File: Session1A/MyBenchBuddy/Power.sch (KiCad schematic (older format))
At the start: 11 parts

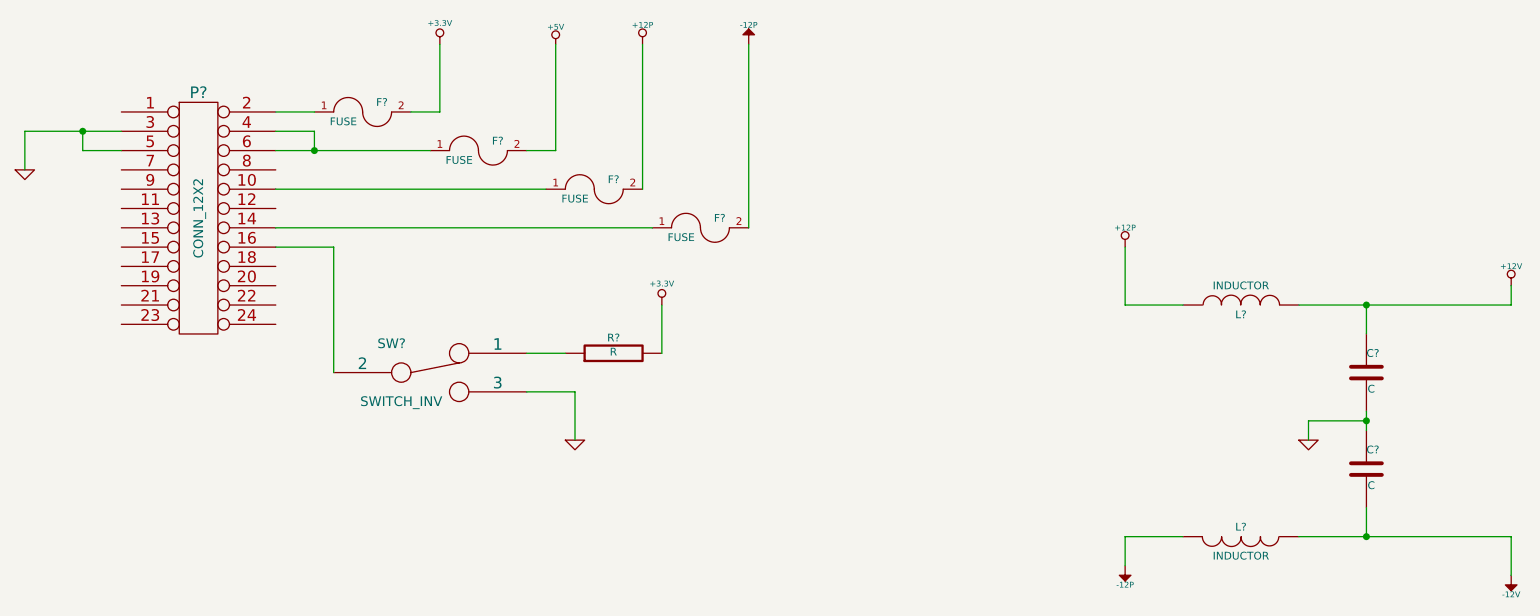
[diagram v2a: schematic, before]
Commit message: Revisiting The Current/Fan Module
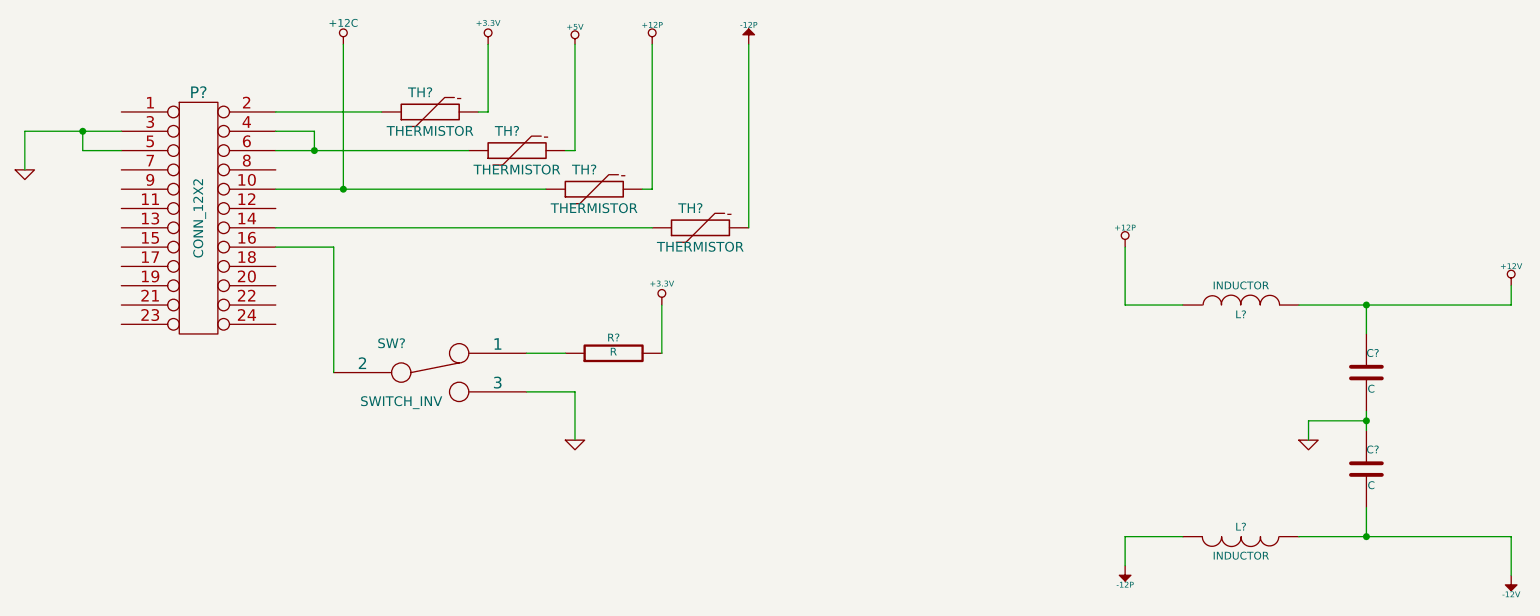
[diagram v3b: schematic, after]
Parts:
- removed F? (x4): FUSE, ~, symbol FUSE
- added TH? (x4): THERMISTOR, ~, symbol THERMISTOR
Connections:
- net +12P: now also TH?.2
- net +3.3V: now also TH?.2
- net +5V: now also TH?.2
- net -12P: now also TH?.2
- net +12C: now reaches P?.10 (P10)
- net +12C: now also TH?.1
- net at P?.14 (P14): now also TH?.1
- net at P?.2 (P2): now also TH?.1
- net at P?.4 (P4), P?.6 (P6): now also TH?.1
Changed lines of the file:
@@
 $Descr A4 11693 8268
 encoding utf-8
-Sheet 5 9
+Sheet 3 9
 Title ""
-Date "26 feb 2014"
+Date "1 mar 2014"
 Rev ""
 Comp ""
@@
 $EndComp
 Wire Wire Line
-	1400 1550 900  1550
+	900  1550 1400 1550
 Wire Wire Line
 	900  1550 900  1750
@@
 L +3.3V #PWR?
 U 1 1 52F9B474
-P 3050 1100
-F 0 "#PWR?" H 3050 1060 30  0001 C CNN
-F 1 "+3.3V" H 3050 1210 30  0000 C CNN
-F 2 "" H 3050 1100 60  0000 C CNN
-F 3 "" H 3050 1100 60  0000 C CNN
-	1    3050 1100
+P 3300 1100
+F 0 "#PWR?" H 3300 1060 30  0001 C CNN
+F 1 "+3.3V" H 3300 1210 30  0000 C CNN
+F 2 "" H 3300 1100 60  0000 C CNN
+F 3 "" H 3300 1100 60  0000 C CNN
+	1    3300 1100
 	1    0    0    -1
 $EndComp
@@
 L +5V #PWR?
 U 1 1 52F9B617
-P 3650 1100
-F 0 "#PWR?" H 3650 1190 20  0001 C CNN
-F 1 "+5V" H 3650 1190 30  0000 C CNN
-F 2 "" H 3650 1100 60  0000 C CNN
-F 3 "" H 3650 1100 60  0000 C CNN
-	1    3650 1100
-	1    0    0    -1
-$EndComp
-$Comp
-L FUSE F?
-U 1 1 52F9BC63
-P 2650 1450
-F 0 "F?" H 2750 1500 40  0000 C CNN
-F 1 "FUSE" H 2550 1400 40  0000 C CNN
-F 2 "~" H 2650 1450 60  0000 C CNN
-F 3 "~" H 2650 1450 60  0000 C CNN
-	1    2650 1450
-	1    0    0    -1
-$EndComp
-$Comp
-L FUSE F?
-U 1 1 52F9BC70
-P 3250 1650
-F 0 "F?" H 3350 1700 40  0000 C CNN
-F 1 "FUSE" H 3150 1600 40  0000 C CNN
-F 2 "~" H 3250 1650 60  0000 C CNN
-F 3 "~" H 3250 1650 60  0000 C CNN
-	1    3250 1650
-	1    0    0    -1
-$EndComp
-$Comp
-L FUSE F?
-U 1 1 52F9BC76
-P 3850 1850
-F 0 "F?" H 3950 1900 40  0000 C CNN
-F 1 "FUSE" H 3750 1800 40  0000 C CNN
-F 2 "~" H 3850 1850 60  0000 C CNN
-F 3 "~" H 3850 1850 60  0000 C CNN
-	1    3850 1850
-	1    0    0    -1
-$EndComp
-$Comp
-L FUSE F?
-U 1 1 52F9BC7C
-P 4400 2050
-F 0 "F?" H 4500 2100 40  0000 C CNN
-F 1 "FUSE" H 4300 2000 40  0000 C CNN
-F 2 "~" H 4400 2050 60  0000 C CNN
-F 3 "~" H 4400 2050 60  0000 C CNN
-	1    4400 2050
+P 3750 1100
+F 0 "#PWR?" H 3750 1190 20  0001 C CNN
+F 1 "+5V" H 3750 1190 30  0000 C CNN
+F 2 "" H 3750 1100 60  0000 C CNN
+F 3 "" H 3750 1100 60  0000 C CNN
+	1    3750 1100
 	1    0    0    -1
 $EndComp
@@
 $EndComp
 Wire Wire Line
-	2200 1450 2400 1450
-Wire Wire Line
-	2900 1450 3050 1450
-Wire Wire Line
-	3050 1450 3050 1100
+	2200 1450 2750 1450
+Wire Wire Line
+	3250 1450 3300 1450
 Wire Wire Line
 	2200 1550 2400 1550
@@
 	2400 1550 2400 1650
 Wire Wire Line
-	2200 1650 3000 1650
+	2200 1650 3200 1650
 Connection ~ 2400 1650
 Wire Wire Line
-	3500 1650 3650 1650
-Wire Wire Line
-	3650 1650 3650 1100
+	3700 1650 3750 1650
 Wire Wire Line
 	2200 1850 3600 1850
 Wire Wire Line
 	4150 2050 2200 2050
-Wire Wire Line
-	4100 1850 4100 1100
 Wire Wire Line
 	4650 2050 4650 1100
@@
 L +12P #PWR?
 U 1 1 52F9C39A
-P 4100 1100
-F 0 "#PWR?" H 4100 1070 30  0001 C CNN
-F 1 "+12P" H 4100 1200 30  0000 C CNN
-F 2 "" H 4100 1100 60  0000 C CNN
-F 3 "" H 4100 1100 60  0000 C CNN
-	1    4100 1100
+P 4150 1100
+F 0 "#PWR?" H 4150 1070 30  0001 C CNN
+F 1 "+12P" H 4150 1200 30  0000 C CNN
+F 2 "" H 4150 1100 60  0000 C CNN
+F 3 "" H 4150 1100 60  0000 C CNN
+	1    4150 1100
 	1    0    0    -1
 $EndComp
@@
 	7500 3650 8600 3650
 Wire Wire Line
-	7850 3100 7850 3000
+	7850 3000 7850 3100
 Wire Wire Line
 	6900 2450 6600 2450
@@
 	-1   0    0    1
 $EndComp
+Wire Wire Line
+	3300 1450 3300 1100
+Wire Wire Line
+	2550 1850 2550 1100
+Connection ~ 2550 1850
+$Comp
+L +12C #PWR?
+U 1 1 53118C21
+P 2550 1100
+F 0 "#PWR?" H 2550 1070 30  0001 C CNN
+F 1 "+12C" H 2550 1210 40  0000 C CNN
+F 2 "" H 2550 1100 60  0000 C CNN
+F 3 "" H 2550 1100 60  0000 C CNN
+	1    2550 1100
+	1    0    0    -1
+$EndComp
+Wire Wire Line
+	3750 1650 3750 1100
+$Comp
+L THERMISTOR TH?
+U 1 1 53119958
+P 3000 1450
+F 0 "TH?" V 3100 1500 50  0000 C CNN
+F 1 "THERMISTOR" V 2900 1450 50  0000 C CNN
+F 2 "~" H 3000 1450 60  0000 C CNN
+F 3 "~" H 3000 1450 60  0000 C CNN
+	1    3000 1450
+	0    -1   -1   0
+$EndComp
+$Comp
+L THERMISTOR TH?
+U 1 1 531199C4
+P 3450 1650
+F 0 "TH?" V 3550 1700 50  0000 C CNN
+F 1 "THERMISTOR" V 3350 1650 50  0000 C CNN
+F 2 "~" H 3450 1650 60  0000 C CNN
+F 3 "~" H 3450 1650 60  0000 C CNN
+	1    3450 1650
+	0    -1   -1   0
+$EndComp
+$Comp
+L THERMISTOR TH?
+U 1 1 531199CA
+P 3850 1850
+F 0 "TH?" V 3950 1900 50  0000 C CNN
+F 1 "THERMISTOR" V 3750 1850 50  0000 C CNN
+F 2 "~" H 3850 1850 60  0000 C CNN
+F 3 "~" H 3850 1850 60  0000 C CNN
+	1    3850 1850
+	0    -1   -1   0
+$EndComp
+$Comp
+L THERMISTOR TH?
+U 1 1 531199D0
+P 4400 2050
+F 0 "TH?" V 4500 2100 50  0000 C CNN
+F 1 "THERMISTOR" V 4300 2050 50  0000 C CNN
+F 2 "~" H 4400 2050 60  0000 C CNN
+F 3 "~" H 4400 2050 60  0000 C CNN
+	1    4400 2050
+	0    -1   -1   0
+$EndComp
+Wire Wire Line
+	4150 1100 4150 1850
+Wire Wire Line
+	4150 1850 4100 1850
 $EndSCHEMATC

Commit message: initial
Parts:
- gave numbers to parts that had none: 11
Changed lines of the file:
@@
 Sheet 3 9
 Title ""
-Date "1 mar 2014"
+Date "15 mar 2014"
 Rev ""
 Comp ""
@@
 $EndDescr
 $Comp
-L CONN_12X2 P?
+L CONN_12X2 P1
 U 1 1 52F9B2D8
 P 1800 2000
-F 0 "P?" H 1800 2650 60  0000 C CNN
+F 0 "P1" H 1800 2650 60  0000 C CNN
 F 1 "CONN_12X2" V 1800 2000 50  0000 C CNN
 F 2 "" H 1800 2000 60  0000 C CNN
@@
 	900  1550 900  1750
 $Comp
-L GND #PWR?
+L GND #PWR3
 U 1 1 52F9B2F7
 P 900 1750
-F 0 "#PWR?" H 900 1750 30  0001 C CNN
+F 0 "#PWR3" H 900 1750 30  0001 C CNN
 F 1 "GND" H 900 1680 30  0001 C CNN
 F 2 "" H 900 1750 60  0000 C CNN
@@
 $EndComp
 $Comp
-L +3.3V #PWR?
+L +3.3V #PWR5
 U 1 1 52F9B474
 P 3300 1100
-F 0 "#PWR?" H 3300 1060 30  0001 C CNN
+F 0 "#PWR5" H 3300 1060 30  0001 C CNN
 F 1 "+3.3V" H 3300 1210 30  0000 C CNN
 F 2 "" H 3300 1100 60  0000 C CNN
@@
 $EndComp
 $Comp
-L +5V #PWR?
+L +5V #PWR6
 U 1 1 52F9B617
 P 3750 1100
-F 0 "#PWR?" H 3750 1190 20  0001 C CNN
+F 0 "#PWR6" H 3750 1190 20  0001 C CNN
 F 1 "+5V" H 3750 1190 30  0000 C CNN
 F 2 "" H 3750 1100 60  0000 C CNN
@@
 $EndComp
 $Comp
-L SWITCH_INV SW?
+L SWITCH_INV SW1
 U 1 1 52F9BE18
 P 3000 2800
-F 0 "SW?" H 2800 2950 50  0000 C CNN
+F 0 "SW1" H 2800 2950 50  0000 C CNN
 F 1 "SWITCH_INV" H 2850 2650 50  0000 C CNN
 F 2 "~" H 3000 2800 60  0000 C CNN
@@
 	4650 2050 4650 1100
 $Comp
-L +12P #PWR?
+L +12P #PWR8
 U 1 1 52F9C39A
 P 4150 1100
-F 0 "#PWR?" H 4150 1070 30  0001 C CNN
+F 0 "#PWR8" H 4150 1070 30  0001 C CNN
 F 1 "+12P" H 4150 1200 30  0000 C CNN
 F 2 "" H 4150 1100 60  0000 C CNN
@@
 $EndComp
 $Comp
-L -12P #PWR?
+L -12P #PWR10
 U 1 1 52F9C3A9
 P 4650 1100
-F 0 "#PWR?" H 4650 1230 20  0001 C CNN
+F 0 "#PWR10" H 4650 1230 20  0001 C CNN
 F 1 "-12P" H 4650 1200 30  0000 C CNN
 F 2 "" H 4650 1100 60  0000 C CNN
@@
 	3750 2900 3750 3150
 $Comp
-L GND #PWR?
+L GND #PWR7
 U 1 1 52F9CAE5
 P 3750 3150
-F 0 "#PWR?" H 3750 3150 30  0001 C CNN
+F 0 "#PWR7" H 3750 3150 30  0001 C CNN
 F 1 "GND" H 3750 3080 30  0001 C CNN
 F 2 "" H 3750 3150 60  0000 C CNN
@@
 $EndComp
 $Comp
-L R R?
+L R R7
 U 1 1 52F9CE4D
 P 3950 2700
-F 0 "R?" V 4030 2700 40  0000 C CNN
+F 0 "R7" V 4030 2700 40  0000 C CNN
 F 1 "R" V 3957 2701 40  0000 C CNN
 F 2 "~" V 3880 2700 30  0000 C CNN
@@
 	4200 2700 4200 2450
 $Comp
-L +3.3V #PWR?
+L +3.3V #PWR9
 U 1 1 52F9CE88
 P 4200 2450
-F 0 "#PWR?" H 4200 2410 30  0001 C CNN
+F 0 "#PWR9" H 4200 2410 30  0001 C CNN
 F 1 "+3.3V" H 4200 2560 30  0000 C CNN
 F 2 "" H 4200 2450 60  0000 C CNN
@@
 $EndComp
 $Comp
-L +12P #PWR?
+L +12P #PWR11
 U 1 1 52F9D03E
 P 6600 2150
-F 0 "#PWR?" H 6600 2120 30  0001 C CNN
+F 0 "#PWR11" H 6600 2120 30  0001 C CNN
 F 1 "+12P" H 6600 2250 30  0000 C CNN
 F 2 "" H 6600 2150 60  0000 C CNN
@@
 $EndComp
 $Comp
-L -12P #PWR?
+L -12P #PWR12
 U 1 1 52F9D044
 P 6600 3800
-F 0 "#PWR?" H 6600 3930 20  0001 C CNN
+F 0 "#PWR12" H 6600 3930 20  0001 C CNN
 F 1 "-12P" H 6600 3900 30  0000 C CNN
 F 2 "" H 6600 3800 60  0000 C CNN
@@
 $EndComp
 $Comp
-L GND #PWR?
+L GND #PWR13
 U 1 1 52F9D20E
 P 7550 3150
-F 0 "#PWR?" H 7550 3150 30  0001 C CNN
+F 0 "#PWR13" H 7550 3150 30  0001 C CNN
 F 1 "GND" H 7550 3080 30  0001 C CNN
 F 2 "" H 7550 3150 60  0000 C CNN
@@
 $EndComp
 $Comp
-L INDUCTOR L?
+L INDUCTOR L1
 U 1 1 52F9D3C6
 P 7200 2450
-F 0 "L?" V 7150 2450 40  0000 C CNN
+F 0 "L1" V 7150 2450 40  0000 C CNN
 F 1 "INDUCTOR" V 7300 2450 40  0000 C CNN
 F 2 "~" H 7200 2450 60  0000 C CNN
@@
 $EndComp
 $Comp
-L INDUCTOR L?
+L INDUCTOR L2
 U 1 1 52F9D3E2
 P 7200 3650
-F 0 "L?" V 7150 3650 40  0000 C CNN
+F 0 "L2" V 7150 3650 40  0000 C CNN
 F 1 "INDUCTOR" V 7300 3650 40  0000 C CNN
 F 2 "~" H 7200 3650 60  0000 C CNN
@@
 $EndComp
 $Comp
-L C C?
+L C C1
 U 1 1 52F9D3EA
 P 7850 2800
-F 0 "C?" H 7850 2900 40  0000 L CNN
+F 0 "C1" H 7850 2900 40  0000 L CNN
 F 1 "C" H 7856 2715 40  0000 L CNN
 F 2 "~" H 7888 2650 30  0000 C CNN
@@
 $EndComp
 $Comp
-L C C?
+L C C2
 U 1 1 52F9D3F7
 P 7850 3300
-F 0 "C?" H 7850 3400 40  0000 L CNN
+F 0 "C2" H 7850 3400 40  0000 L CNN
 F 1 "C" H 7856 3215 40  0000 L CNN
 F 2 "~" H 7888 3150 30  0000 C CNN
@@
 Connection ~ 7850 2450
 $Comp
-L +12V #PWR?
+L +12V #PWR14
 U 1 1 52F9D6C6
 P 8600 2350
-F 0 "#PWR?" H 8600 2300 20  0001 C CNN
+F 0 "#PWR14" H 8600 2300 20  0001 C CNN
 F 1 "+12V" H 8600 2450 30  0000 C CNN
 F 2 "" H 8600 2350 60  0000 C CNN
@@
 Connection ~ 7850 3650
 $Comp
-L -12V #PWR?
+L -12V #PWR15
 U 1 1 52F9D8BC
 P 8600 3850
-F 0 "#PWR?" H 8600 3980 20  0001 C CNN
+F 0 "#PWR15" H 8600 3980 20  0001 C CNN
 F 1 "-12V" H 8600 3950 30  0000 C CNN
 F 2 "" H 8600 3850 60  0000 C CNN
@@
 Connection ~ 2550 1850
 $Comp
-L +12C #PWR?
+L +12C #PWR4
 U 1 1 53118C21
 P 2550 1100
-F 0 "#PWR?" H 2550 1070 30  0001 C CNN
+F 0 "#PWR4" H 2550 1070 30  0001 C CNN
 F 1 "+12C" H 2550 1210 40  0000 C CNN
 F 2 "" H 2550 1100 60  0000 C CNN
@@
 	3750 1650 3750 1100
 $Comp
-L THERMISTOR TH?
+L THERMISTOR TH1
 U 1 1 53119958
 P 3000 1450
-F 0 "TH?" V 3100 1500 50  0000 C CNN
+F 0 "TH1" V 3100 1500 50  0000 C CNN
 F 1 "THERMISTOR" V 2900 1450 50  0000 C CNN
 F 2 "~" H 3000 1450 60  0000 C CNN
@@
 $EndComp
 $Comp
-L THERMISTOR TH?
+L THERMISTOR TH2
 U 1 1 531199C4
 P 3450 1650
-F 0 "TH?" V 3550 1700 50  0000 C CNN
+F 0 "TH2" V 3550 1700 50  0000 C CNN
 F 1 "THERMISTOR" V 3350 1650 50  0000 C CNN
 F 2 "~" H 3450 1650 60  0000 C CNN
@@
 $EndComp
 $Comp
-L THERMISTOR TH?
+L THERMISTOR TH3
 U 1 1 531199CA
 P 3850 1850
-F 0 "TH?" V 3950 1900 50  0000 C CNN
+F 0 "TH3" V 3950 1900 50  0000 C CNN
 F 1 "THERMISTOR" V 3750 1850 50  0000 C CNN
 F 2 "~" H 3850 1850 60  0000 C CNN
@@
 $EndComp
 $Comp
-L THERMISTOR TH?
+L THERMISTOR TH4
 U 1 1 531199D0
 P 4400 2050
-F 0 "TH?" V 4500 2100 50  0000 C CNN
+F 0 "TH4" V 4500 2100 50  0000 C CNN
 F 1 "THERMISTOR" V 4300 2050 50  0000 C CNN
 F 2 "~" H 4400 2050 60  0000 C CNN
